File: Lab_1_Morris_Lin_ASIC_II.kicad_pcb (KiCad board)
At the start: 4 copper layers, 100 x 100 mm, 7 parts, among them J1 Q1_Header

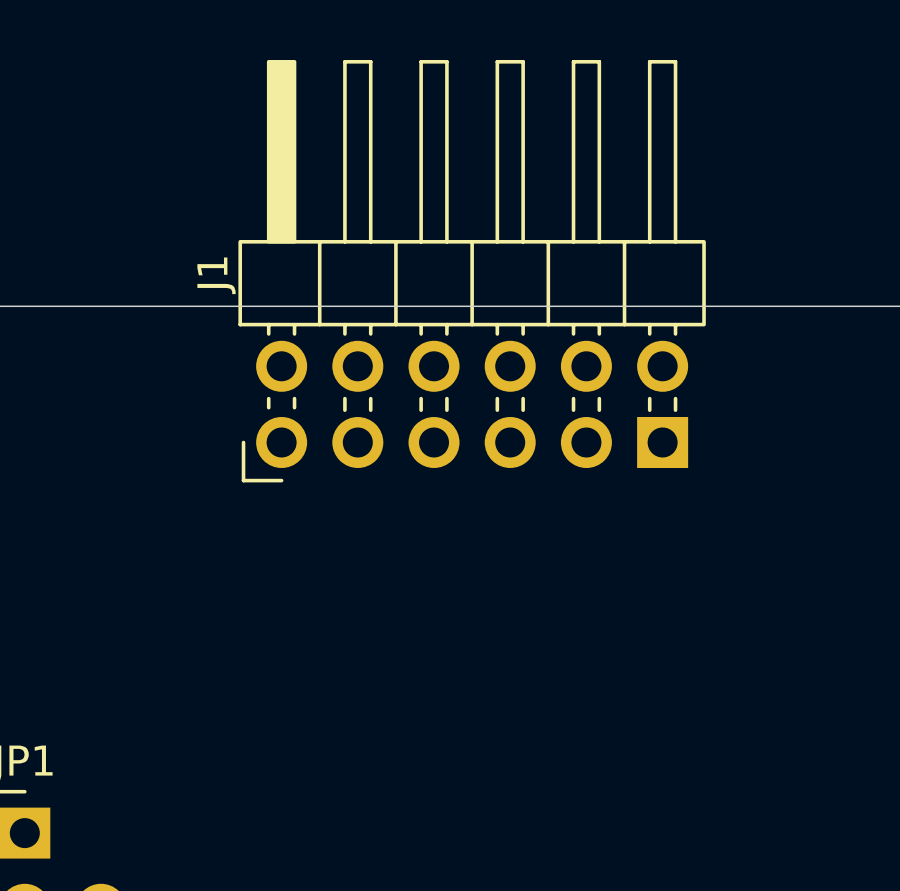
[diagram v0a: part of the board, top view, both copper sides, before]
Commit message: Swapped to 1-of-4 Demux IC setup
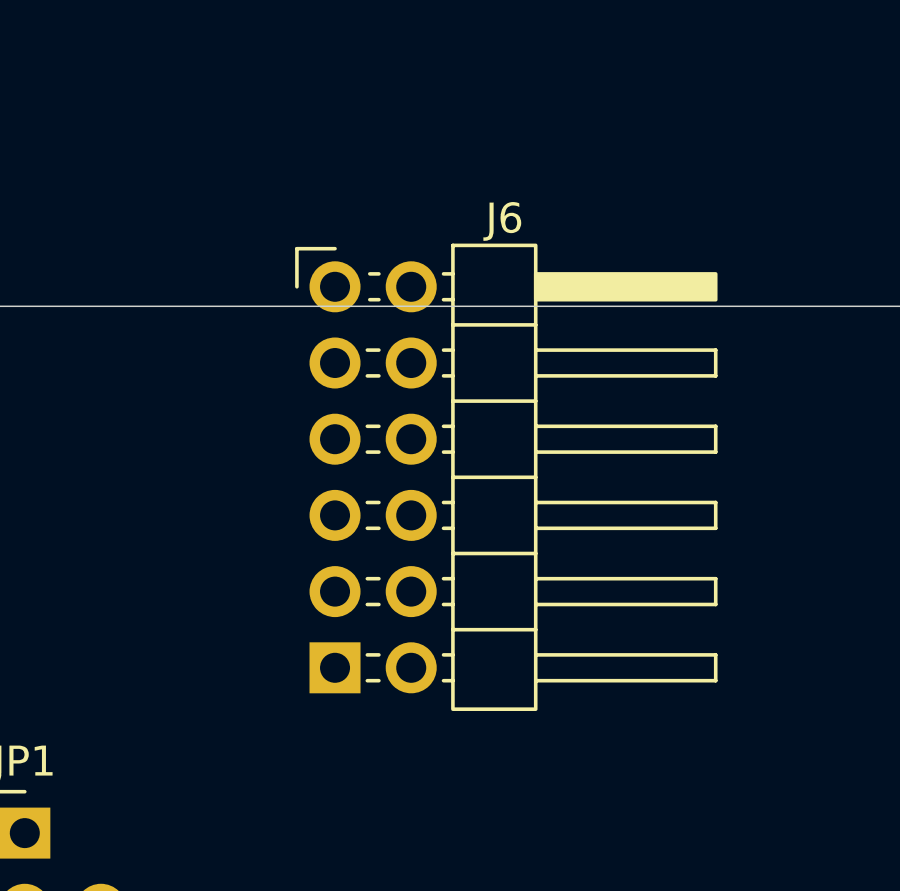
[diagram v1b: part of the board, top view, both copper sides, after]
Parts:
- removed J1: Q1_Header, ASIC_II:PinHeader_2x06_P2.54mm_Horizontal
- added J6: Q1_Header, ASIC_II:PinHeader_2x06_P2.54mm_Horizontal, F.Cu at (60.3, 39.4)
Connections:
- U1 pad 1: unconnected-(U1-Pad1) -> /s_clk_Q1
- U1 pad 11: unconnected-(U1-Pad11) -> /s_out_Q3
- U1 pad 12: unconnected-(U1-Pad12) -> /s_update_Q3
- U1 pad 13: unconnected-(U1-Pad13) -> /s_in_Q3
- U1 pad 14: unconnected-(U1-Pad14) -> /s_clk_Q3
- U1 pad 15: unconnected-(U1-Pad15) -> /CLK_Q3
- U1 pad 17: unconnected-(U1-Pad17) -> /RSTn_Q3
- U1 pad 18: unconnected-(U1-Pad18) -> /Krdy_Q3
- U1 pad 19: unconnected-(U1-Pad19) -> /Drdy_Q3
- U1 pad 2: unconnected-(U1-Pad2) -> /s_in_Q1
- U1 pad 21: unconnected-(U1-Pad21) -> /BSY_Q3
- U1 pad 22: unconnected-(U1-Pad22) -> /BSY_Q4
- U1 pad 24: unconnected-(U1-Pad24) -> /Drdy_Q4
- U1 pad 25: unconnected-(U1-Pad25) -> /Krdy_Q4
- U1 pad 26: unconnected-(U1-Pad26) -> /RSTn_Q4
- U1 pad 28: unconnected-(U1-Pad28) -> /CLK_Q4
- U1 pad 29: unconnected-(U1-Pad29) -> /s_clk_Q4
- U1 pad 3: unconnected-(U1-Pad3) -> /s_update_Q1
- U1 pad 30: unconnected-(U1-Pad30) -> /s_in_Q4
- U1 pad 31: unconnected-(U1-Pad31) -> /s_update_Q4
- U1 pad 32: unconnected-(U1-Pad32) -> /s_out_Q4
- U1 pad 34: unconnected-(U1-Pad34) -> /Kvld_Q4
- U1 pad 35: unconnected-(U1-Pad35) -> /Dvld_Q4
- U1 pad 36: unconnected-(U1-Pad36) -> /Dvld_Q2
- U1 pad 37: unconnected-(U1-Pad37) -> /Kvld_Q2
- U1 pad 39: unconnected-(U1-Pad39) -> /s_out_Q2
- U1 pad 4: unconnected-(U1-Pad4) -> /s_out_Q1
- U1 pad 40: unconnected-(U1-Pad40) -> /s_update_Q2
- U1 pad 41: unconnected-(U1-Pad41) -> /s_in_Q2
- U1 pad 42: unconnected-(U1-Pad42) -> /s_clk_Q2
- U1 pad 43: unconnected-(U1-Pad43) -> /CLK_Q2
- U1 pad 45: unconnected-(U1-Pad45) -> /RSTn_Q2
- U1 pad 46: unconnected-(U1-Pad46) -> /Krdy_Q2
- U1 pad 47: unconnected-(U1-Pad47) -> /Drdy_Q2
- U1 pad 49: unconnected-(U1-Pad49) -> /BSY_Q2
- U1 pad 50: unconnected-(U1-Pad50) -> /BSY_Q1
- U1 pad 52: unconnected-(U1-Pad52) -> /Drdy_Q1
- U1 pad 53: unconnected-(U1-Pad53) -> /Krdy_Q1
- U1 pad 54: unconnected-(U1-Pad54) -> /RSTn_Q1
- U1 pad 56: unconnected-(U1-Pad56) -> /CLK_Q1
- U1 pad 6: unconnected-(U1-Pad6) -> /Kvld_Q1
- U1 pad 7: unconnected-(U1-Pad7) -> /Dvld_Q1
- U1 pad 8: unconnected-(U1-Pad8) -> /Dvld_Q3
- U1 pad 9: unconnected-(U1-Pad9) -> /Kvld_Q3

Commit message: Starting routing
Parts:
- added C1: 1u, Capacitor_SMD:C_1206_3216Metric_Pad1.33x1.80mm_HandSolder, F.Cu at (111.7, 116.4)
- added C10: 0.1u, Capacitor_SMD:C_1206_3216Metric_Pad1.33x1.80mm_HandSolder, F.Cu at (84.9, 121.8)
- added C11: 0.1u, Capacitor_SMD:C_1206_3216Metric_Pad1.33x1.80mm_HandSolder, F.Cu at (88.1, 95.9)
- added C12: 0.1u, Capacitor_SMD:C_1206_3216Metric_Pad1.33x1.80mm_HandSolder, F.Cu at (88.7, 121.8)
- added C2: 1u, Capacitor_SMD:C_1206_3216Metric_Pad1.33x1.80mm_HandSolder, F.Cu at (127.8, 106.1)
- added C3: 1u, Capacitor_SMD:C_1206_3216Metric_Pad1.33x1.80mm_HandSolder, F.Cu at (118.1, 121.3)
- added C4: 1u, Capacitor_SMD:C_1206_3216Metric_Pad1.33x1.80mm_HandSolder, F.Cu at (133.0, 100.9)
- added C5: 10u, Capacitor_SMD:C_1206_3216Metric_Pad1.33x1.80mm_HandSolder, F.Cu at (49.6, 62.1)
- added C6: 0.1u, Capacitor_SMD:C_1206_3216Metric_Pad1.33x1.80mm_HandSolder, F.Cu at (70.0, 109.8)
- added C7: 0.1u, Capacitor_SMD:C_1206_3216Metric_Pad1.33x1.80mm_HandSolder, F.Cu at (80.7, 95.9)
- added C8: 0.1u, Capacitor_SMD:C_1206_3216Metric_Pad1.33x1.80mm_HandSolder, F.Cu at (81.1, 121.8)
- added C9: 0.1u, Capacitor_SMD:C_1206_3216Metric_Pad1.33x1.80mm_HandSolder, F.Cu at (84.4, 95.9)
- added D1: Q1, LED_SMD:LED_1206_3216Metric_Pad1.42x1.75mm_HandSolder, F.Cu at (126.9, 81.9)
- added D2: Q2, LED_SMD:LED_1206_3216Metric_Pad1.42x1.75mm_HandSolder, F.Cu at (126.9, 77.6)
- added D3: Q3, LED_SMD:LED_1206_3216Metric_Pad1.42x1.75mm_HandSolder, F.Cu at (126.9, 73.3)
- added D4: Q4, LED_SMD:LED_1206_3216Metric_Pad1.42x1.75mm_HandSolder, F.Cu at (126.9, 69.0)
- added D5: PTVS3V3S1UR,115, Diode_SMD:Nexperia_CFP3_SOD-123W, F.Cu at (49.9, 66.7)
- added D6: VDDPOC, LED_SMD:LED_1206_3216Metric_Pad1.42x1.75mm_HandSolder, F.Cu at (101.5, 126.1)
- added D7: ~{OE}, LED_SMD:LED_1206_3216Metric_Pad1.42x1.75mm_HandSolder, F.Cu at (46.0, 121.0)
- added D8: VDDPST, LED_SMD:LED_1206_3216Metric_Pad1.42x1.75mm_HandSolder, F.Cu at (49.6, 52.2)
- added F1: SMDH1206B025TF, Fuse:Fuse_1206_3216Metric_Pad1.42x1.75mm_HandSolder, F.Cu at (44.7, 65.4)
- added IC1: 74CBTLV3253D,118, ASIC_II:SOIC127P600X175-16N, F.Cu at (77.8, 59.6)
- added IC2: 74CBTLV3253D,118, ASIC_II:SOIC127P600X175-16N, F.Cu at (60.3, 81.2)
- added IC3: 74CBTLV3253D,118, ASIC_II:SOIC127P600X175-16N, F.Cu at (90.7, 81.2)
- added IC4: 74CBTLV3253D,118, ASIC_II:SOIC127P600X175-16N, F.Cu at (103.5, 59.8)
- added IC5: 74CBTLV3253D,118, ASIC_II:SOIC127P600X175-16N, F.Cu at (121.3, 59.7)
- added IC6: 74CBTLV3253D,118, ASIC_II:SOIC127P600X175-16N, F.Cu at (132.4, 59.7)
- added J1: VDDPST_External, Connector:Banana_Jack_2Pin, F.Cu at (47.7, 80.4)
- added J2: PMOD_A, ASIC_II:PinHeader_2x06_P2.54mm_Horizontal, F.Cu at (72.2, 45.1)
- added J3: PMOD_B, ASIC_II:PinHeader_2x06_P2.54mm_Horizontal, F.Cu at (95.0, 45.1)
- added J4: VDD_Qn External, Connector:Banana_Jack_1Pin, F.Cu at (133.7, 117.2)
- added J5: VDDPST External, Connector:Banana_Jack_1Pin, F.Cu at (112.5, 131.6)
- added J7: PMOD_B, ASIC_II:PinHeader_VertNum_2x06_P2.54mm_Vertical, F.Cu at (126.7, 45.1)
- added JP10: Jumper_3_Open, Connector_PinHeader_2.54mm:PinHeader_1x03_P2.54mm_Vertical, F.Cu at (121.5, 107.2)
- added JP2: Jumper_3_Open, Connector_PinHeader_2.54mm:PinHeader_1x03_P2.54mm_Vertical, F.Cu at (128.6, 94.9)
- added JP3: Jumper_3_Open, Connector_PinHeader_2.54mm:PinHeader_1x03_P2.54mm_Vertical, F.Cu at (123.8, 122.8)
- added JP4: Jumper_3_Open, Connector_PinHeader_2.54mm:PinHeader_1x03_P2.54mm_Vertical, F.Cu at (121.5, 89.2)
- added JP5: Jumper_3_Open, Connector_PinHeader_2.54mm:PinHeader_1x03_P2.54mm_Vertical, F.Cu at (59.1, 126.3)
- added JP6: Jumper_3_Open, Connector_PinHeader_2.54mm:PinHeader_1x03_P2.54mm_Vertical, F.Cu at (52.9, 125.7)
- added JP7: Jumper_3_Open, Connector_PinHeader_2.54mm:PinHeader_1x03_P2.54mm_Vertical, F.Cu at (121.5, 95.2)
- added JP8: Jumper_3_Open, Connector_PinHeader_2.54mm:PinHeader_1x03_P2.54mm_Vertical, F.Cu at (121.5, 101.2)
- added JP9: Jumper_3_Open, Connector_PinHeader_2.54mm:PinHeader_1x03_P2.54mm_Vertical, F.Cu at (59.1, 120.2)
- added Q1: BSS138, Package_TO_SOT_SMD:SOT-23, F.Cu at (101.5, 121.3)
- added R1: 470, Resistor_SMD:R_1206_3216Metric_Pad1.30x1.75mm_HandSolder, F.Cu at (134.4, 81.9)
- added R10: 10k, Resistor_SMD:R_1206_3216Metric_Pad1.30x1.75mm_HandSolder, F.Cu at (60.0, 114.0)
- added R11: 10k, Resistor_SMD:R_1206_3216Metric_Pad1.30x1.75mm_HandSolder, F.Cu at (87.3, 55.4)
- added R12: 10k, Resistor_SMD:R_1206_3216Metric_Pad1.30x1.75mm_HandSolder, F.Cu at (68.5, 55.3)
- added R13: 10k, Resistor_SMD:R_1206_3216Metric_Pad1.30x1.75mm_HandSolder, F.Cu at (69.3, 75.9)
- added R14: 10k, Resistor_SMD:R_1206_3216Metric_Pad1.30x1.75mm_HandSolder, F.Cu at (101.0, 75.8)
- added R15: 10k, Resistor_SMD:R_1206_3216Metric_Pad1.30x1.75mm_HandSolder, F.Cu at (75.6, 75.9)
- added R16: 10k, Resistor_SMD:R_1206_3216Metric_Pad1.30x1.75mm_HandSolder, F.Cu at (87.3, 58.8)
- added R17: 10k, Resistor_SMD:R_1206_3216Metric_Pad1.30x1.75mm_HandSolder, F.Cu at (68.5, 58.8)
- added R18: 10k, Resistor_SMD:R_1206_3216Metric_Pad1.30x1.75mm_HandSolder, F.Cu at (69.3, 79.6)
- added R19: 10k, Resistor_SMD:R_1206_3216Metric_Pad1.30x1.75mm_HandSolder, F.Cu at (100.9, 79.5)
- added R2: 470, Resistor_SMD:R_1206_3216Metric_Pad1.30x1.75mm_HandSolder, F.Cu at (134.4, 77.6)
- added R20: 10k, Resistor_SMD:R_1206_3216Metric_Pad1.30x1.75mm_HandSolder, F.Cu at (75.6, 79.6)
- added R21: 10k, Resistor_SMD:R_1206_3216Metric_Pad1.30x1.75mm_HandSolder, F.Cu at (87.3, 62.3)
- added R22: 10k, Resistor_SMD:R_1206_3216Metric_Pad1.30x1.75mm_HandSolder, F.Cu at (68.5, 62.3)
- added R23: 10k, Resistor_SMD:R_1206_3216Metric_Pad1.30x1.75mm_HandSolder, F.Cu at (69.3, 83.2)
- added R24: 10k, Resistor_SMD:R_1206_3216Metric_Pad1.30x1.75mm_HandSolder, F.Cu at (100.8, 83.1)
- added R25: 10k, Resistor_SMD:R_1206_3216Metric_Pad1.30x1.75mm_HandSolder, F.Cu at (75.6, 83.2)
- added R26: 10k, Resistor_SMD:R_1206_3216Metric_Pad1.30x1.75mm_HandSolder, F.Cu at (87.3, 65.8)
- added R27: 10k, Resistor_SMD:R_1206_3216Metric_Pad1.30x1.75mm_HandSolder, F.Cu at (68.5, 65.8)
- added R28: 10k, Resistor_SMD:R_1206_3216Metric_Pad1.30x1.75mm_HandSolder, F.Cu at (69.3, 86.8)
- added R29: 10k, Resistor_SMD:R_1206_3216Metric_Pad1.30x1.75mm_HandSolder, F.Cu at (100.9, 86.8)
- added R3: 470, Resistor_SMD:R_1206_3216Metric_Pad1.30x1.75mm_HandSolder, F.Cu at (134.4, 73.3)
- added R30: 10k, Resistor_SMD:R_1206_3216Metric_Pad1.30x1.75mm_HandSolder, F.Cu at (75.6, 86.8)
- added R31: 10k, Resistor_SMD:R_1206_3216Metric_Pad1.30x1.75mm_HandSolder, F.Cu at (111.5, 55.4)
- added R32: 10k, Resistor_SMD:R_1206_3216Metric_Pad1.30x1.75mm_HandSolder, F.Cu at (96.1, 55.2)
- added R33: 10k, Resistor_SMD:R_1206_3216Metric_Pad1.30x1.75mm_HandSolder, F.Cu at (111.5, 59.1)
- added R34: 10k, Resistor_SMD:R_1206_3216Metric_Pad1.30x1.75mm_HandSolder, F.Cu at (96.1, 59.0)
- added R35: 10k, Resistor_SMD:R_1206_3216Metric_Pad1.30x1.75mm_HandSolder, F.Cu at (111.5, 62.8)
- added R36: 10k, Resistor_SMD:R_1206_3216Metric_Pad1.30x1.75mm_HandSolder, F.Cu at (96.1, 62.8)
- added R37: 10k, Resistor_SMD:R_1206_3216Metric_Pad1.30x1.75mm_HandSolder, F.Cu at (111.5, 66.5)
- added R38: 10k, Resistor_SMD:R_1206_3216Metric_Pad1.30x1.75mm_HandSolder, F.Cu at (96.1, 66.6)
- added R4: 470, Resistor_SMD:R_1206_3216Metric_Pad1.30x1.75mm_HandSolder, F.Cu at (134.4, 69.0)
- added R5: 10k, Resistor_SMD:R_1206_3216Metric_Pad1.30x1.75mm_HandSolder, F.Cu at (63.3, 131.0)
- added R6: 10k, Resistor_SMD:R_1206_3216Metric_Pad1.30x1.75mm_HandSolder, F.Cu at (57.2, 131.0)
- added R7: 470, Resistor_SMD:R_1206_3216Metric_Pad1.30x1.75mm_HandSolder, F.Cu at (106.0, 121.8)
- added R8: 470, Resistor_SMD:R_1206_3216Metric_Pad1.30x1.75mm_HandSolder, F.Cu at (46.0, 125.7)
- added R9: 470, Resistor_SMD:R_1206_3216Metric_Pad1.30x1.75mm_HandSolder, F.Cu at (49.6, 57.4)
- added TP1: TestPoint, TestPoint:TestPoint_Loop_D2.54mm_Drill1.5mm_Beaded, F.Cu at (117.3, 112.6)
- added TP2: TestPoint, TestPoint:TestPoint_Loop_D2.54mm_Drill1.5mm_Beaded, F.Cu at (44.0, 59.5)
- added TP3: TestPoint, TestPoint:TestPoint_Loop_D2.54mm_Drill1.5mm_Beaded, F.Cu at (128.2, 88.9)
- added TP4: TestPoint, TestPoint:TestPoint_Loop_D2.54mm_Drill1.5mm_Beaded, F.Cu at (134.8, 88.9)
- added TP5: TestPoint, TestPoint:TestPoint_Loop_D2.54mm_Drill1.5mm_Beaded, F.Cu at (125.3, 112.6)
- added TP6: TestPoint, TestPoint:TestPoint_Loop_D2.54mm_Drill1.5mm_Beaded, F.Cu at (44.0, 51.5)
- added U1: TLV75710PDBV, Package_TO_SOT_SMD:SOT-23-5, F.Cu at (111.0, 121.8)
- added U2: TLV75710PDBV, Package_TO_SOT_SMD:SOT-23-5, F.Cu at (133.4, 107.0)
- J6: value Q1_Header -> PMOD_A; footprint ASIC_II:PinHeader_2x06_P2.54mm_Horizontal -> ASIC_II:PinHeader_VertNum_2x06_P2.54mm_Vertical
- JP1: value Jumper_SP4T_Open -> Jumper_3_Open; footprint ASIC_II:PinHeader_SP4T_1x03_P2.54mm_Vertical -> Connector_PinHeader_2.54mm:PinHeader_1x03_P2.54mm_Vertical
- moved U3 19.7 mm to (83.5, 108.6)
- moved JP1 14.2 mm to (50.4, 71.7), turned to -90 degrees
- moved J6 8.21 mm to (66.2, 45.1), turned to -90 degrees
- renumbered U1 to U3
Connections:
- J6 pad 1: /PMOD_B1 -> /PMOD_A1
- J6 pad 10: /PMOD_B10 -> /PMOD_A10
- J6 pad 11: GND -> unconnected-(J6-Pin_11-Pad11)
- J6 pad 12: VDD -> GND
- J6 pad 2: /PMOD_B2 -> /PMOD_A2
- J6 pad 3: /PMOD_B3 -> /PMOD_A3
- J6 pad 4: /PMOD_B4 -> /PMOD_A4
- J6 pad 5: GND -> unconnected-(J6-Pin_5-Pad5)
- J6 pad 6: VDD -> GND
- J6 pad 7: /PMOD_B7 -> /PMOD_A7
- J6 pad 8: /PMOD_B8 -> /PMOD_A8
- J6 pad 9: /PMOD_B9 -> /PMOD_A9
- JP1 pad 1: unconnected-(JP1-A-Pad1) -> VDDPMOD
- JP1 pad 2: unconnected-(JP1-B-Pad2) -> Net-(JP1-C)
- JP1 pad 3: unconnected-(JP1-C-Pad3) -> Net-(J1-Pin_1)
- U3 pad 16: VSS -> GND
- U3 pad 33: VSSPST -> GND
- U3 pad 44: VSS -> GND
- U3 pad 5: VSSPST -> GND
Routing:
- net VDDPST: vias 0 -> 14
- added copper zone on B.Cu, net GND
- added copper zone on F.Cu, net GND
- added copper zone on In2.Cu, net GND
- added copper zone on F.Cu, net Net-(J1-Pin_1)
- added copper zone on F.Cu, net Net-(J5-Pin_1)
- added copper zone on F.Cu, net Net-(JP1-C)
- added copper zone on F.Cu, net VDDPST
- added copper zone on In1.Cu, net VDDPST

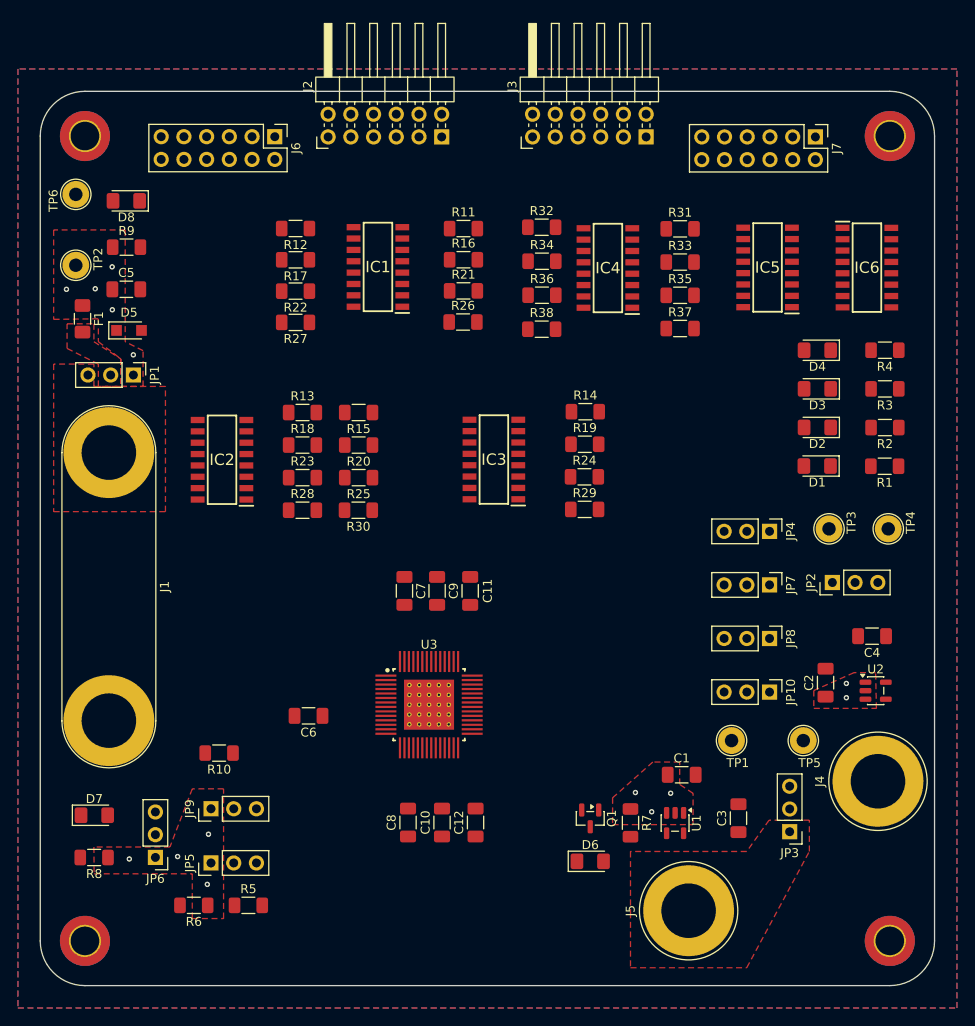
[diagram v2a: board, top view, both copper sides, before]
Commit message: Fanned out ASIC pins
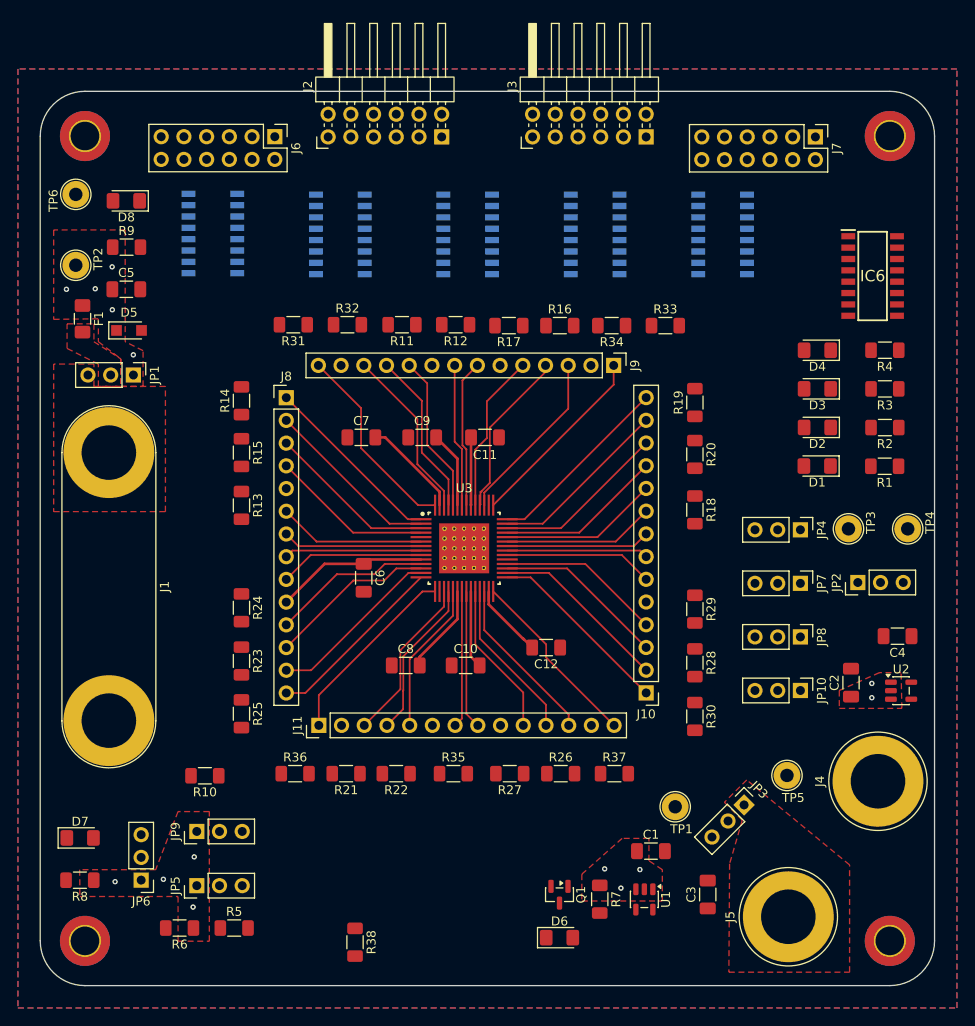
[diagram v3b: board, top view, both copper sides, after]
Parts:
- added J10: Conn_01x14, Connector_PinHeader_2.54mm:PinHeader_1x14_P2.54mm_Vertical, F.Cu at (107.8, 107.3)
- added J11: Conn_01x14, Connector_PinHeader_2.54mm:PinHeader_1x14_P2.54mm_Vertical, F.Cu at (71.2, 110.9)
- added J8: Conn_01x14, Connector_PinHeader_2.54mm:PinHeader_1x14_P2.54mm_Vertical, F.Cu at (67.5, 74.3)
- added J9: Conn_01x14, Connector_PinHeader_2.54mm:PinHeader_1x14_P2.54mm_Vertical, F.Cu at (104.1, 70.7)
- IC1, IC2, IC3, IC4, IC5: moved to B.Cu
- moved R38 71.7 mm to (75.2, 135.2), turned to -90 degrees
- moved R36 60.2 mm to (68.5, 116.3)
- moved R35 59.2 mm to (86.2, 116.3)
- moved R27 55.9 mm to (92.5, 116.3)
- moved R21 55.6 mm to (74.2, 116.3), turned to 180 degrees
- moved R22 55.1 mm to (79.8, 116.3)
- moved R26 51.7 mm to (98.2, 116.3)
- moved R37 50.3 mm to (104.2, 116.3)
- moved R28 47.1 mm to (113.2, 103.9), turned to -90 degrees
- moved R31 44.6 mm to (68.3, 66.1), turned to 180 degrees
- moved R18 44.5 mm to (113.2, 86.8), turned to -90 degrees
- moved R30 44.1 mm to (113.2, 109.9), turned to -90 degrees
- moved R24 41.0 mm to (62.5, 97.8), turned to -90 degrees
- moved R14 38.5 mm to (62.5, 74.6), turned to 90 degrees
- moved R20 37.6 mm to (113.2, 80.6), turned to -90 degrees
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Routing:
- net /CLK_Q1: track 0.00 -> 22.1 mm
- net /CLK_Q2: track 0.00 -> 21.2 mm
- net /CLK_Q3: track 0.00 -> 21.2 mm
- net /s_clk_Q2: track 0.00 -> 21.2 mm
- net /s_clk_Q4: track 0.00 -> 20.9 mm
- net /s_clk_Q1: track 0.00 -> 20.7 mm
- net /CLK_Q4: track 0.00 -> 20.6 mm
- net /s_clk_Q3: track 0.00 -> 20.4 mm
- net /s_in_Q2: track 0.00 -> 20.3 mm
- net /s_in_Q4: track 0.00 -> 20.0 mm
- net /s_in_Q1: track 0.00 -> 19.8 mm
- net /s_in_Q3: track 0.00 -> 19.6 mm
- net /RSTn_Q2: track 0.00 -> 19.5 mm
- net VDD: track 0.00 -> 19.5 mm
- net /s_update_Q2: track 0.00 -> 19.5 mm
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
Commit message: Added keepout and mux side swapping
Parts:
- IC4, IC5: moved to F.Cu
- moved IC2 31.3 mm to (119.1, 56.2), turned to 90 degrees
- moved IC1 30.1 mm to (89.4, 56.2), turned to 90 degrees
- moved IC4 27.5 mm to (74.5, 56.2), turned to -90 degrees
- moved IC3 13.9 mm to (59.6, 56.2), turned to 90 degrees
- moved IC5 12.0 mm to (104.3, 56.2), turned to -90 degrees
- moved J6 1.40 mm to (66.2, 43.7)
- moved J7 1.40 mm to (126.7, 43.7)
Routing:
- net VDD: track 19.5 -> 40.6 mm
- net VDD_Q2: track 7.58 -> 17.0 mm
- net VDD_Q1: track 8.56 -> 16.8 mm
- net VDD_Q4: track 8.68 -> 16.4 mm
- net VDD_Q3: track 10.0 -> 17.3 mm

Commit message: auto1 design
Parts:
- removed J1: VDDPST_External, Connector:Banana_Jack_2Pin
- added J12: VDDPST External, Connector:Banana_Jack_1Pin, F.Cu at (47.8, 111.1)
- added J13: GND External, Connector:Banana_Jack_1Pin, F.Cu at (47.7, 125.5)
- IC1, IC2, IC3: moved to F.Cu
- J5: value VDDPST External -> VDDRING External
- moved JP5 76.2 mm to (44.9, 53.7), turned to 0 degrees
- moved JP9 69.5 mm to (50.4, 53.7), turned to 0 degrees
- moved R5 66.3 mm to (44.6, 69.5), turned to -90 degrees
- moved JP6 64.6 mm to (45.2, 63.9), turned to 90 degrees
- moved R6 58.4 mm to (44.6, 76.2), turned to 90 degrees
- moved IC2 58.3 mm to (61.0, 60.6), turned to 180 degrees
- moved R8 49.3 mm to (49.6, 79.2), turned to 0 degrees
- moved D7 48.9 mm to (49.7, 74.8)
- moved R10 48.0 mm to (48.8, 69.5), turned to -90 degrees
- moved IC4 44.4 mm to (118.7, 60.6), turned to 180 degrees
- moved Q1 34.0 mm to (117.9, 102.3), turned to 0 degrees
- moved D6 33.2 mm to (117.5, 107.7), turned to -90 degrees
- moved JP1 30.8 mm to (50.5, 102.5)
- moved TP6 30.8 mm to (44.1, 82.3)
- moved C5 30.8 mm to (49.7, 92.9)
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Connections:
- J2 pad 12: VDDPMOD -> unconnected-(J2-Pin_12-Pad12)
- J3 pad 12: VDDPMOD -> unconnected-(J3-Pin_12-Pad12)
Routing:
- net /SEL_b1: track 0.00 -> 178.4 mm, vias 0 -> 17
- net /~{OE}: track 0.00 -> 173.0 mm, vias 0 -> 35
- net /SEL_b0: track 0.00 -> 169.4 mm, vias 0 -> 19
- net /s_out_Q4: track 18.3 -> 179.7 mm, vias 0 -> 6
- net /s_clk_Q4: track 20.9 -> 176.6 mm, vias 0 -> 6
- net /s_update_Q4: track 19.2 -> 167.1 mm, vias 0 -> 6
- net /s_in_Q4: track 20.0 -> 130.9 mm, vias 0 -> 6
- net /RSTn_Q3: track 18.7 -> 125.5 mm, vias 0 -> 4
- net /s_update_Q2: track 19.5 -> 124.5 mm, vias 0 -> 4
- net /s_in_Q3: track 19.6 -> 119.1 mm, vias 0 -> 4
- net VDDPMOD: track 0.00 -> 96.4 mm
- net VDD: track 40.6 -> 136.5 mm
- net /BSY_Q4: track 15.5 -> 109.6 mm, vias 0 -> 3
- net /Drdy_Q4: track 17.2 -> 111.2 mm, vias 0 -> 4
- net /CLK_Q1: track 22.1 -> 106.7 mm, vias 0 -> 6
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- removed copper zone on F.Cu, net Net-(J5-Pin_1)
